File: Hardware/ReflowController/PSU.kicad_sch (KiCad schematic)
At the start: 2 parts, among them U1 TSR_1-2450, U2 LD1117S33TR_SOT223

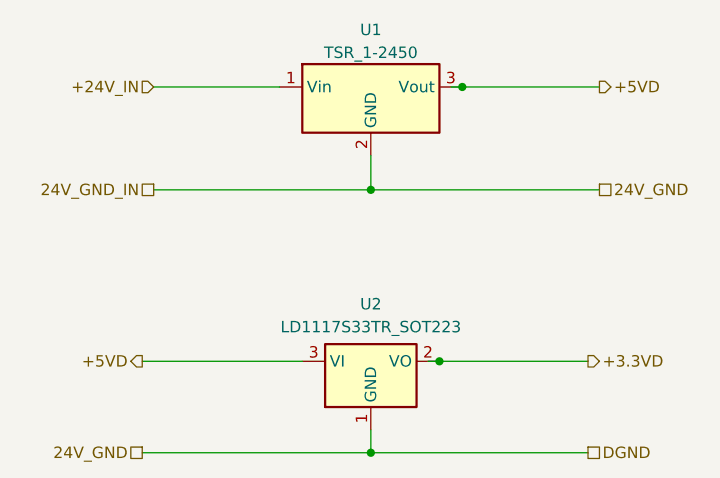
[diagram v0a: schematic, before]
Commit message: finished the io control for the pcb, need to define what is the best way for a remote keypad
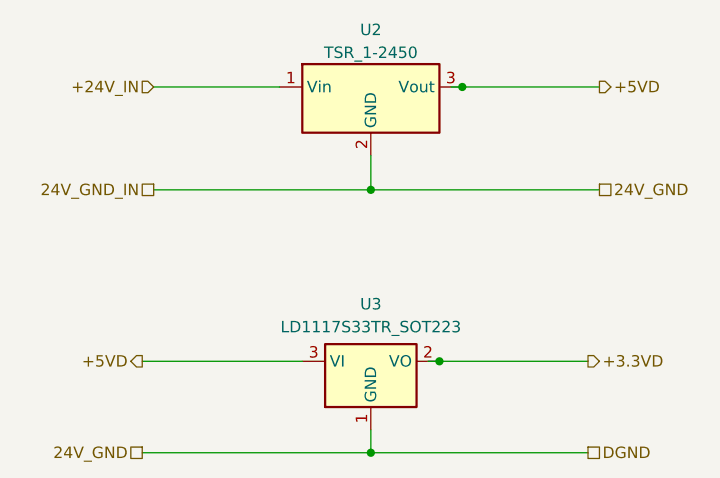
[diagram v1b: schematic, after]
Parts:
- renumbered U1 to U2, U2 to U3
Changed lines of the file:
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@@
   (symbol (lib_id "Regulator_Switching:TSR_1-2450") (at 132.08 27.94 0) (unit 1)
     (in_bom yes) (on_board yes) (dnp no) (fields_autoplaced)
-    (property "Reference" "U1" (at 132.08 19.05 0)
+    (property "Reference" "U2" (at 132.08 19.05 0)
       (effects (font (size 1.27 1.27)))
     )
@@
       (project "ReflowController"
         (path "/2394cc2a-b9b0-4c0b-be11-1fc6085b0d5c/f93d5910-f900-4b81-b729-10d58386d359"
-          (reference "U1") (unit 1)
+          (reference "U2") (unit 1)
         )
       )
@@
   (symbol (lib_id "Regulator_Linear:LD1117S33TR_SOT223") (at 132.08 55.88 0) (unit 1)
     (in_bom yes) (on_board yes) (dnp no) (fields_autoplaced)
-    (property "Reference" "U2" (at 132.08 49.53 0)
+    (property "Reference" "U3" (at 132.08 49.53 0)
       (effects (font (size 1.27 1.27)))
     )
@@
       (project "ReflowController"
         (path "/2394cc2a-b9b0-4c0b-be11-1fc6085b0d5c/f93d5910-f900-4b81-b729-10d58386d359"
-          (reference "U2") (unit 1)
+          (reference "U3") (unit 1)
         )
       )

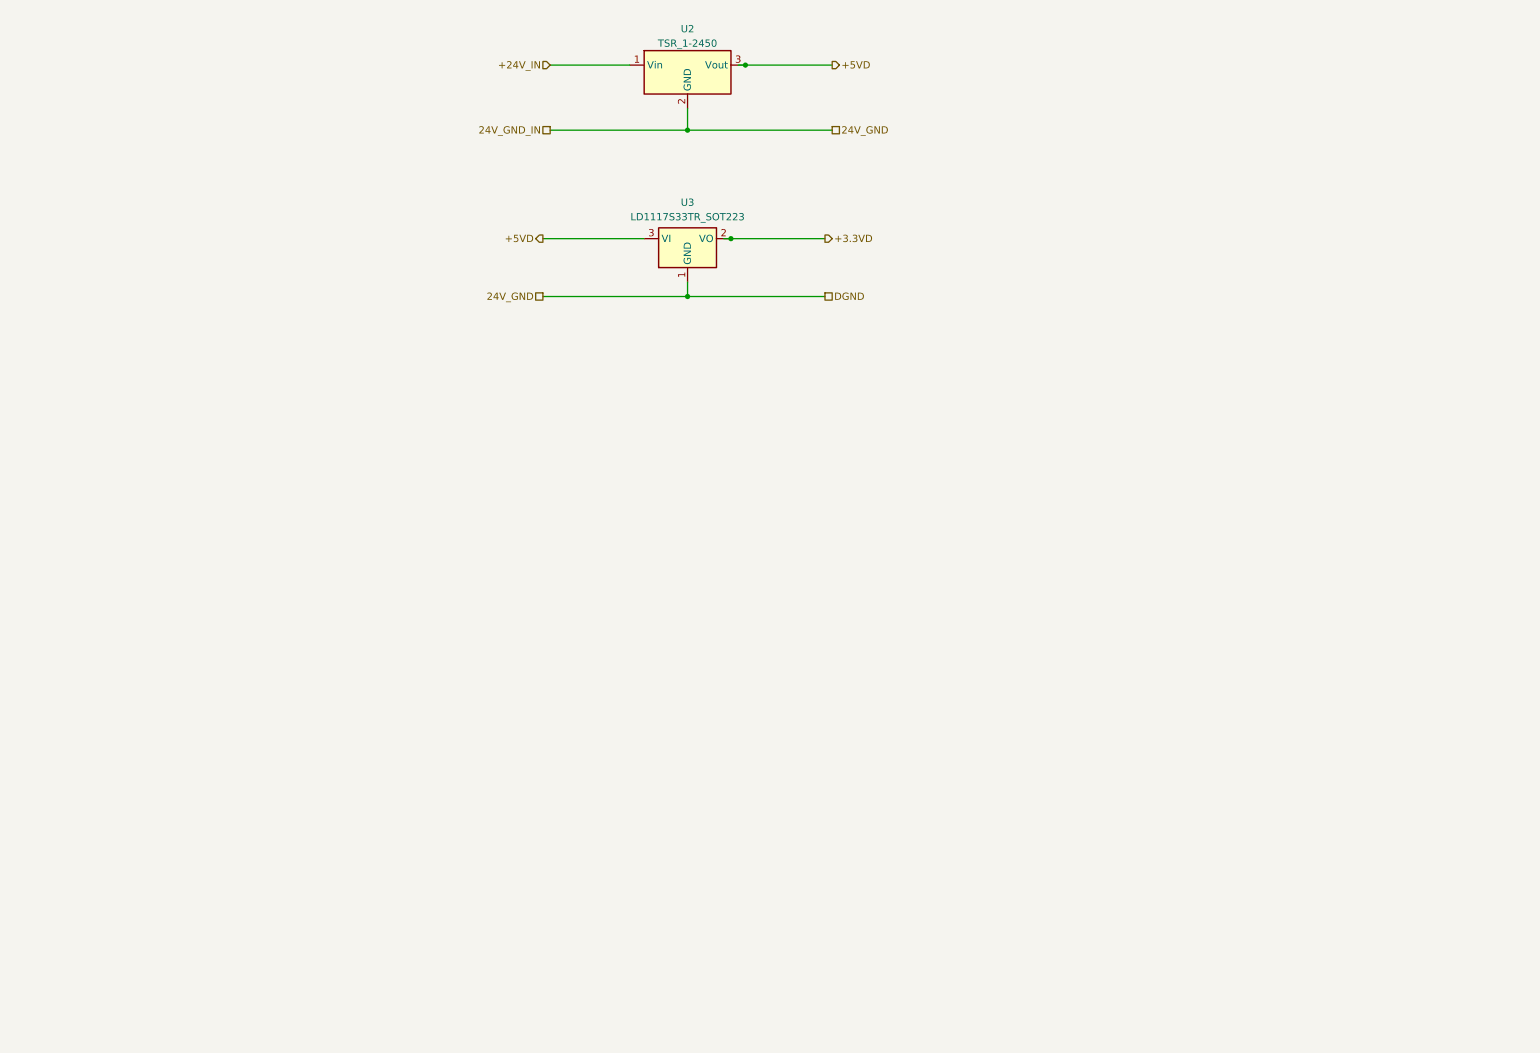
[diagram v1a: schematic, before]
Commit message: Main Schematic rooting and PSU Dqsing ongoing
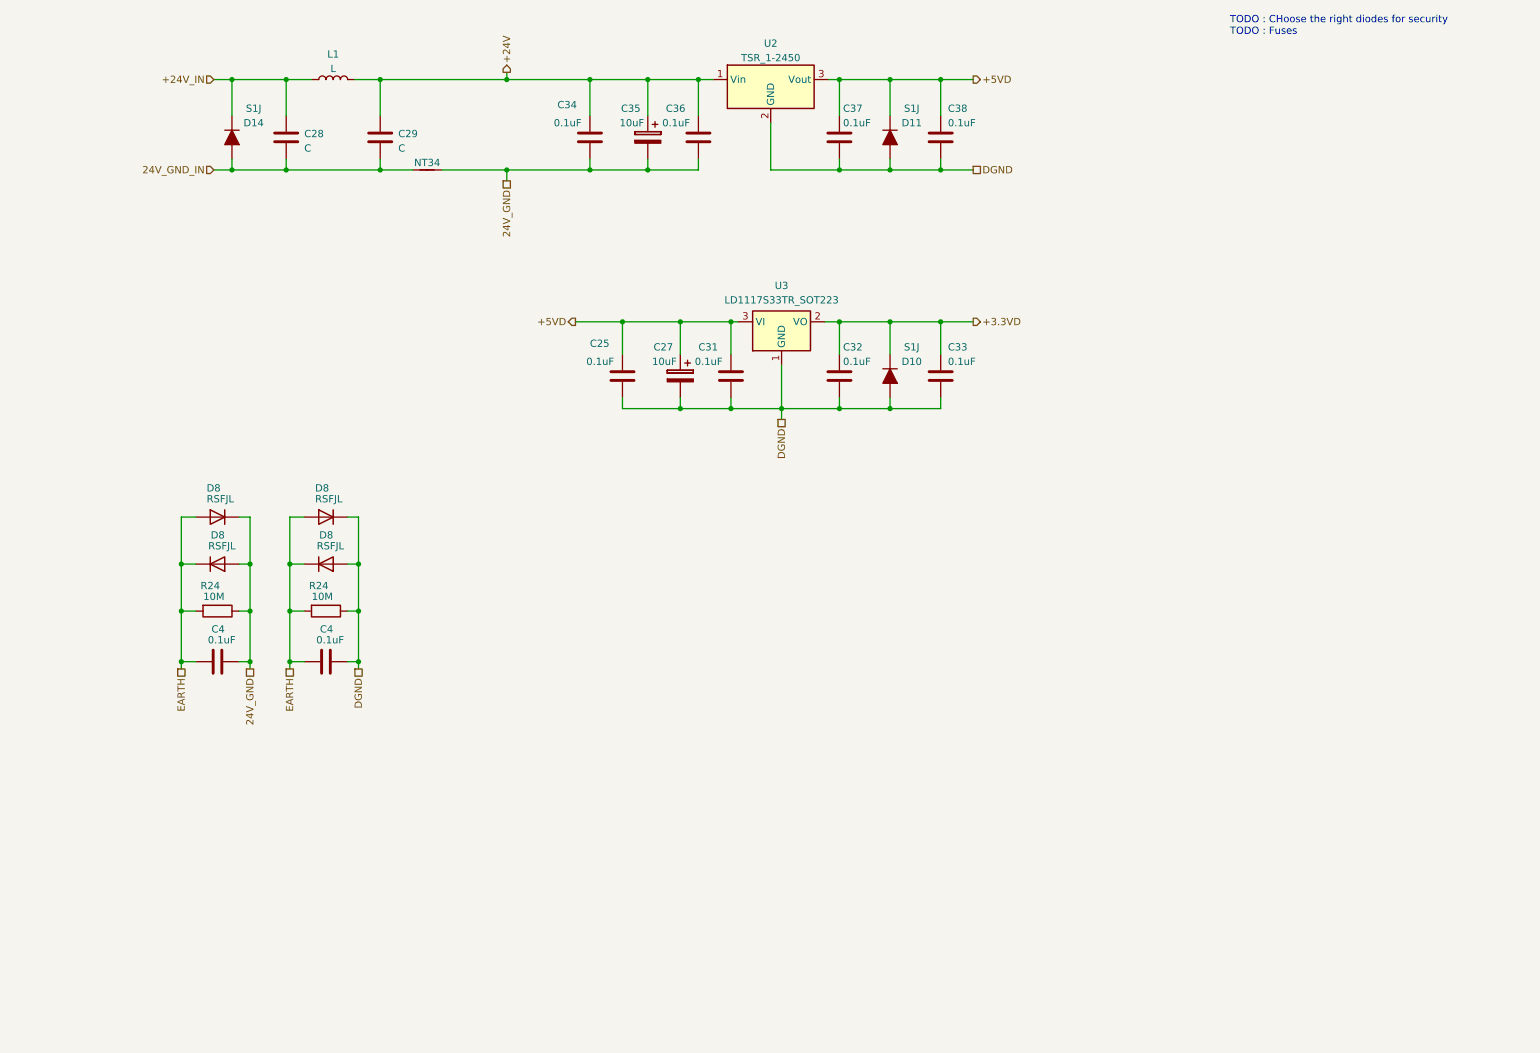
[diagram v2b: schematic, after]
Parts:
- added C25, C33, C34, C38: 0.1uF, Capacitor_THT:C_Rect_L7.2mm_W2.5mm_P5.00mm_FKS2_FKP2_MKS2_MKP2, symbol Ampli50W-rescue:C
- added C27, C35: 10uF, Capacitor_THT:CP_Radial_D5.0mm_P2.00mm, symbol Ampli50W-rescue:CP
- added C28, C29: C, symbol Device:C
- added C31, C32, C36, C37: 0.1uF, Capacitor_SMD:C_1206_3216Metric, symbol Ampli50W-rescue:C
- added C4 (x2): 0.1uF, Capacitor_SMD:C_1206_3216Metric, symbol Device:C
- added D10, D11, D14: S1J, Diode_SMD:D_SMA_Handsoldering, symbol Ampli50W-rescue:D_ALT
- added D8 (x4): RSFJL, Diode_SMD:D_SMA_Handsoldering, symbol Device:D
- added L1: L, symbol Device:L
- added NT34: NetTie_2, NetTie:NetTie-2_SMD_Pad2.0mm, symbol Device:NetTie_2
- added R24 (x2): 10M, Resistor_SMD:R_1206_3216Metric, symbol Device:R
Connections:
- net +24V_IN: now also C28.1, D14.1 (K), L1.1; no longer U2.1 (Vin)
- net +3.3VD: now also C32.2, C33.1, D10.1 (K)
- net +5VD: now also C25.1, C27.1, C31.2, C37.2, C38.1, D11.1 (K)
- net 24V_GND: now also C34.2, C35.2, C36.1, C4.2, D8.1 (K), D8.2 (A), NT34.2, R24.1; no longer U2.2 (GND), U3.1 (GND)
- new net +24V: C29.1, C34.1, C35.1, C36.2, L1.2, U2.1 (Vin)
- new net 24V_GND_IN: C28.2, C29.2, D14.2 (A), NT34.1
- new net DGND: C25.2, C27.2, C31.1, C32.1, C33.2, C37.1, C38.2, C4.2, D10.2 (A), D11.2 (A), D8.1 (K), D8.2 (A), R24.1, U2.2 (GND), U3.1 (GND)
- new net EARTH: C4.1, C4.1, D8.1 (K), D8.1 (K), D8.2 (A), D8.2 (A), R24.2, R24.2
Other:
- note added: "TODO : CHoose the right diodes for security TODO : Fuses"
- moved on the sheet: U2, U3

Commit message: Finished the desing of the PSUand started with the PCB TODO: missing fuse find a solution
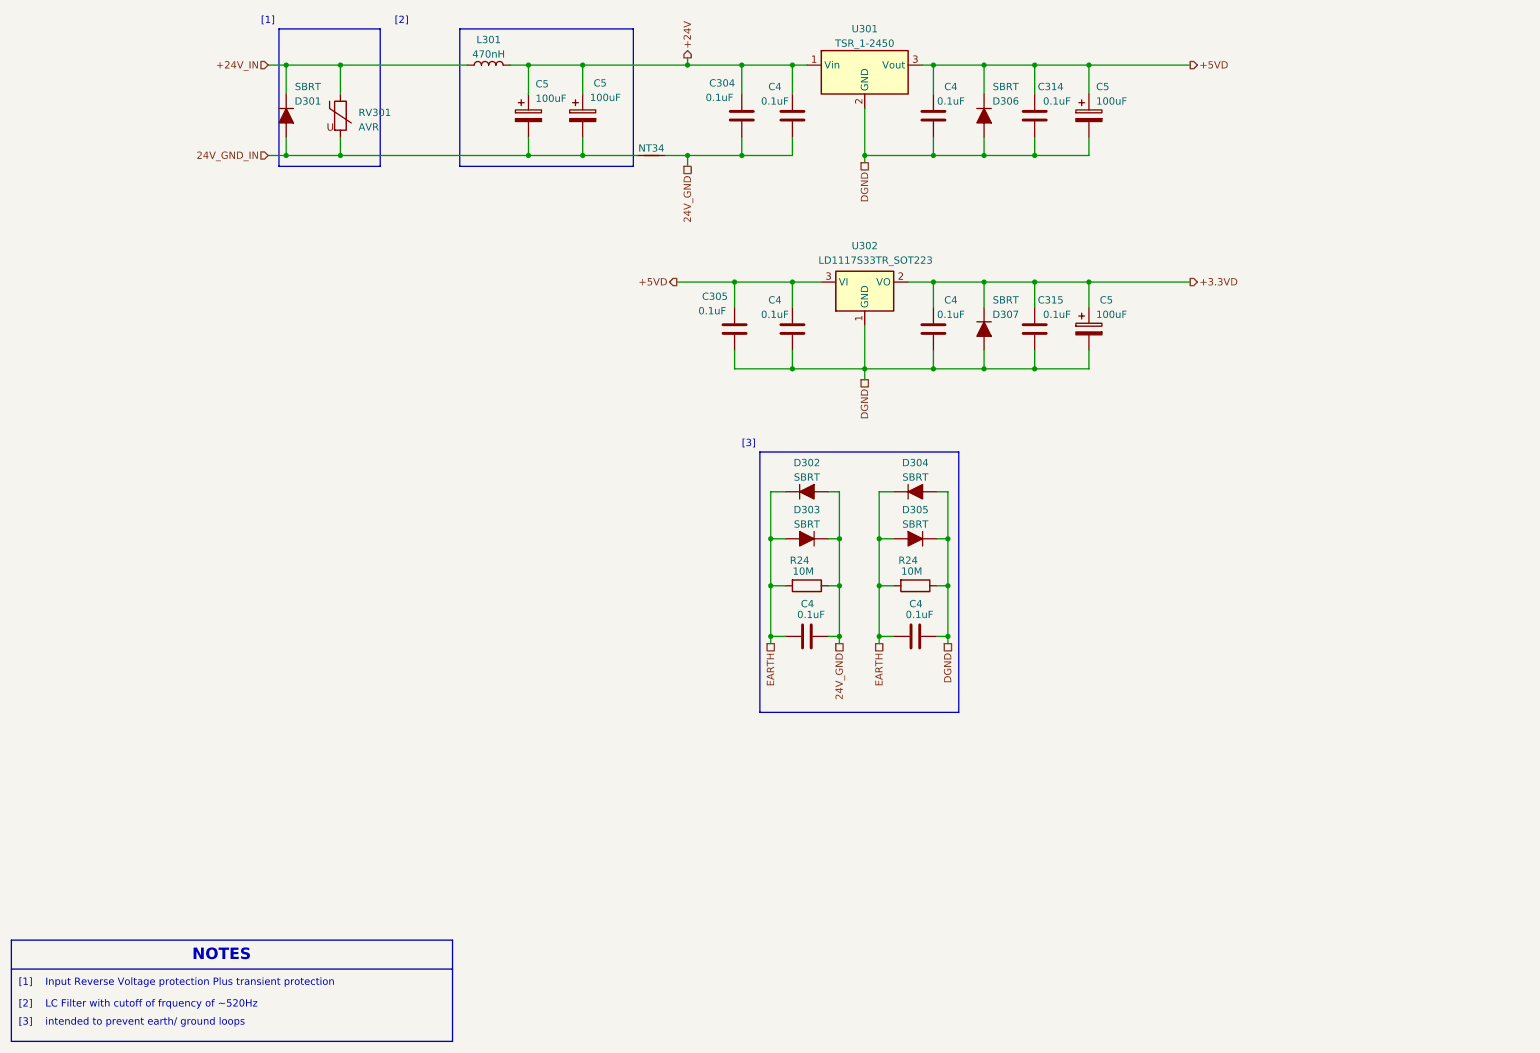
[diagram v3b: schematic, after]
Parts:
- removed C25, C33, C34, C38: 0.1uF, Capacitor_THT:C_Rect_L7.2mm_W2.5mm_P5.00mm_FKS2_FKP2_MKS2_MKP2, symbol Ampli50W-rescue:C
- removed C27, C35: 10uF, Capacitor_THT:CP_Radial_D5.0mm_P2.00mm, symbol Ampli50W-rescue:CP
- removed C28, C29: C, symbol Device:C
- removed C31, C32, C36, C37: 0.1uF, Capacitor_SMD:C_1206_3216Metric, symbol Ampli50W-rescue:C
- removed D10, D14: S1J, Diode_SMD:D_SMA_Handsoldering, symbol Ampli50W-rescue:D_ALT
- removed D8 (x4): RSFJL, Diode_SMD:D_SMA_Handsoldering, symbol Device:D
- added C304, C305, C314, C315: 0.1uF, Capacitor_THT:C_Rect_L7.2mm_W2.5mm_P5.00mm_FKS2_FKP2_MKS2_MKP2, symbol Ampli50W-rescue:C
- added C4 (x4): 0.1uF, Capacitor_SMD:C_1206_3216Metric, symbol Device:C
- added C5 (x4): 100uF, Capacitor_SMD:CP_Elec_8x10.5, symbol Device:C_Polarized
- added D301, D302, D303, D304, D305, D307: SBRT, Diode_SMD:D_SMA_Handsoldering, symbol Ampli50W-rescue:D_ALT
- added RV301: AVR, Resistor_SMD:R_0603_1608Metric_Pad0.98x0.95mm_HandSolder, symbol Device:Varistor
- D306: renamed from D11; value S1J -> SBRT; Digikey S1J-FDICT-ND -> (none); disit (none) -> digikey; disti_no (none) -> SBRT5A50SA-13DICT-ND; man (none) -> diodes; man_no (none) -> SBRT5A50SA-13
- L301: renamed from L1; value L -> 470nH; footprint (none) -> 020_SMD_Inductors:2520; disti (none) -> digikey; disti_no (none) -> 490-10653-2-ND; man (none) -> murata; man_no (none) -> DFE252012P-R47M=P2
- renumbered U2 to U301, U3 to U302
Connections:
- net +24V: now also C304.1, C4.2, C5.1, C5.1
- net +24V_IN: now also D301.1 (K), RV301.1
- net +3.3VD: now also C315.1, C4.2, C5.1, D307.1 (K)
- net +5VD: now also C305.1, C314.1, C4.2, C4.2, C5.1
- net 24V_GND: now also C304.2, C4.1, D302.2 (A), D303.1 (K)
- net 24V_GND_IN: now also C5.2, C5.2, D301.2 (A), RV301.2
- net DGND: now also C305.2, C314.2, C315.2, C4.1, C4.1, C4.1, C5.2, C5.2, D304.2 (A), D305.1 (K), D307.2 (A)
- net EARTH: now also D302.1 (K), D303.2 (A), D304.1 (K), D305.2 (A)
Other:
- note added: "NOTES"
- note added: "[1]"
- note added: "[1] Input Reverse Voltage protection Plus transient protection"
- note added: "[2]"
- note added: "[2] LC Filter with cutoff of frquency of ~520Hz"
- note added: "[3]"
- note added: "[3] intended to prevent earth/ ground loops"
- note removed: "TODO : CHoose the right diodes for security TODO : Fuses"
- moved on the sheet: C4, D306, L301, NT34, R24, U301, U302
